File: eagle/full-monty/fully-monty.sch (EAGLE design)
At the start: 20 parts

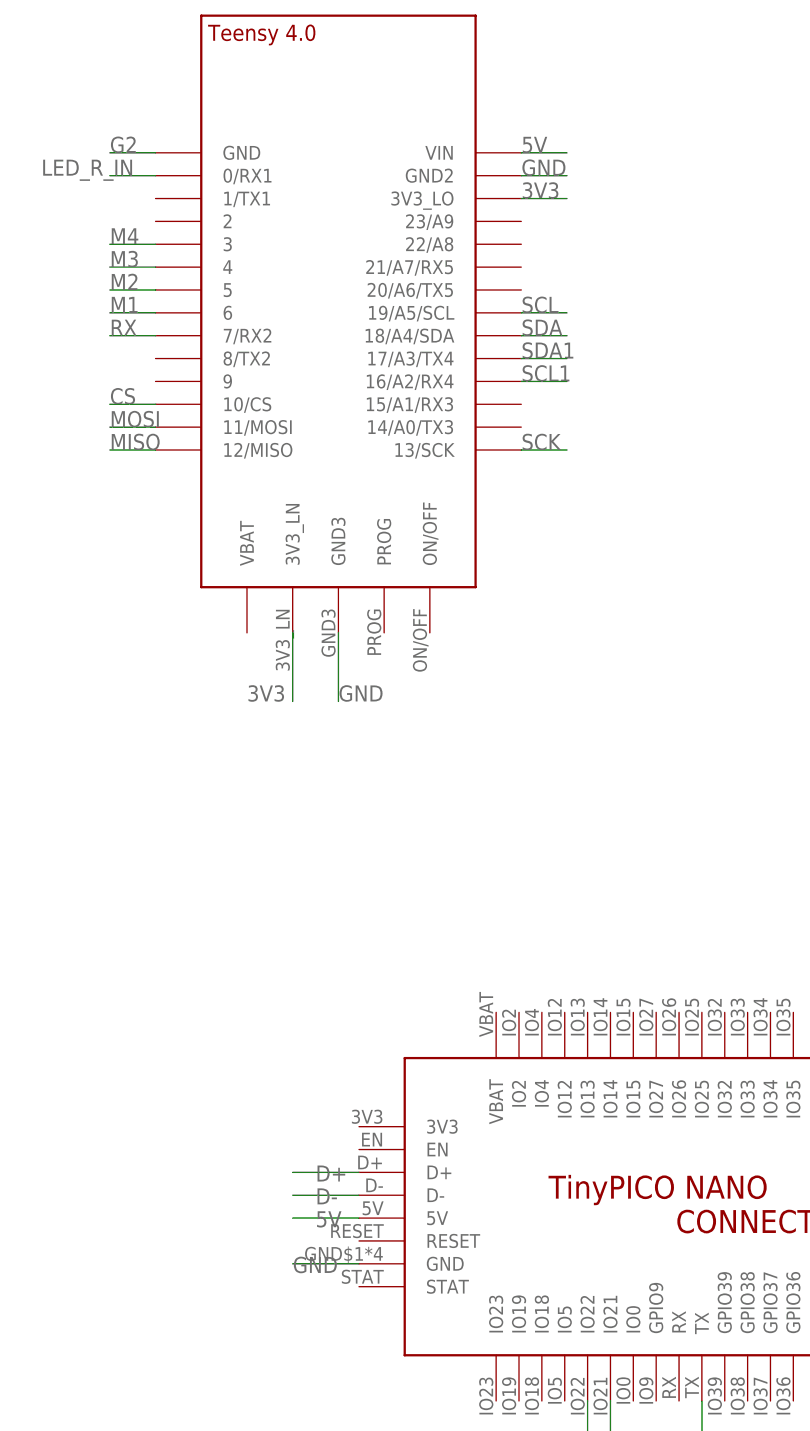
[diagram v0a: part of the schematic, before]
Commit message: modified:   eagle/full-monty/fully-monty.brd
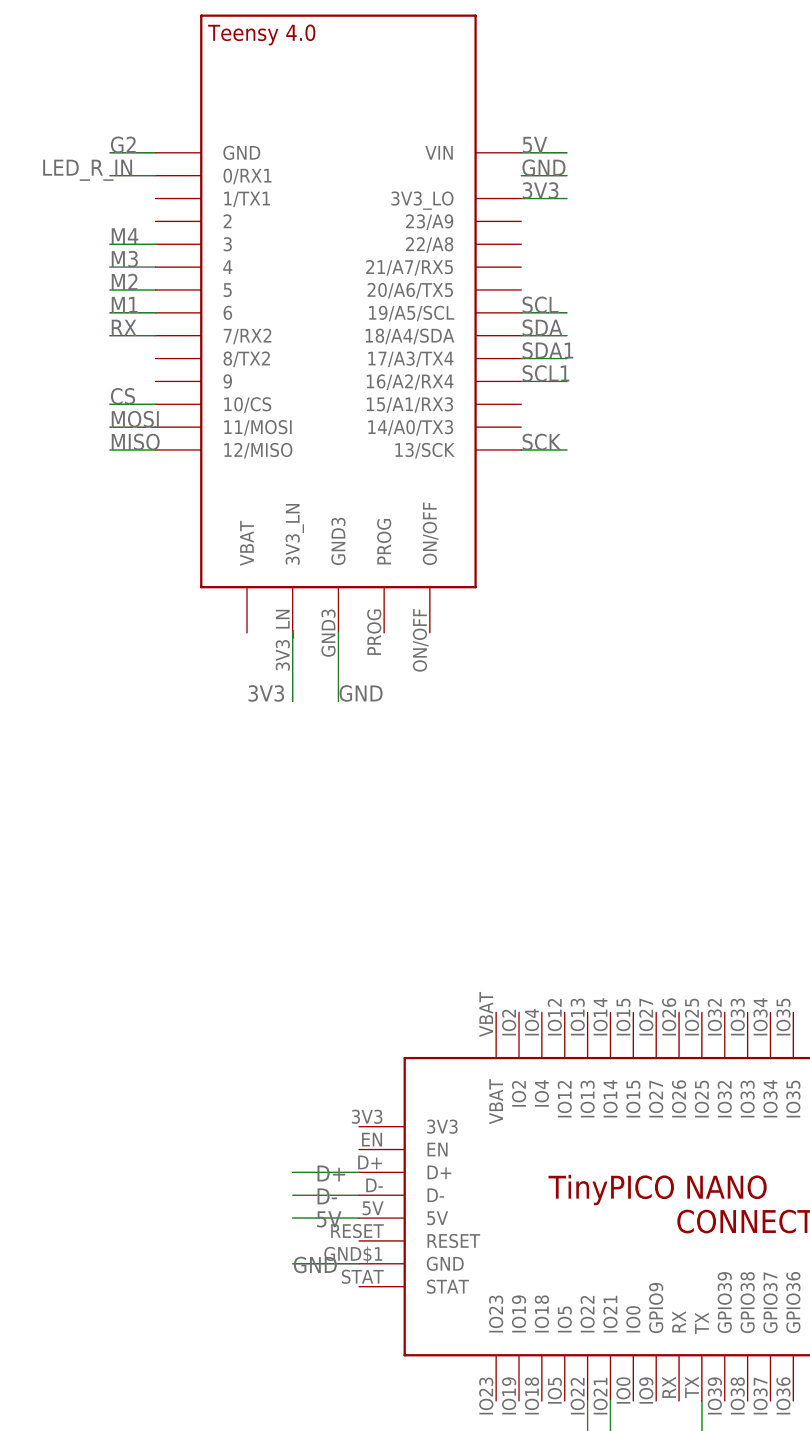
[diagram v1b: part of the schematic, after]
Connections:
- net GND: no longer U$1.GND2
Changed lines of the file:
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@@
 <net name="GND" class="0">
 <segment>
-<pinref part="U$1" gate="G$1" pin="GND2"/>
 <wire x1="93.98" y1="60.96" x2="99.06" y2="60.96" width="0.1524" layer="91"/>
 <label x="93.98" y="60.96" size="1.778" layer="95"/>

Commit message: modified:   fully-monty.brd
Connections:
- net GND: now also U$1.GND2
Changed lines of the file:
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@@
 <net name="GND" class="0">
-<segment>
-<wire x1="93.98" y1="60.96" x2="99.06" y2="60.96" width="0.1524" layer="91"/>
-<label x="93.98" y="60.96" size="1.778" layer="95"/>
-</segment>
 <segment>
 <pinref part="REG" gate="J1" pin="2"/>
@@
 <label x="213.36" y="50.8" size="1.778" layer="95"/>
 </segment>
+<segment>
+<pinref part="U$1" gate="G$1" pin="GND2"/>
+<wire x1="93.98" y1="60.96" x2="99.06" y2="60.96" width="0.1524" layer="91"/>
+<label x="93.98" y="60.96" size="1.778" layer="95"/>
+</segment>
 </net>

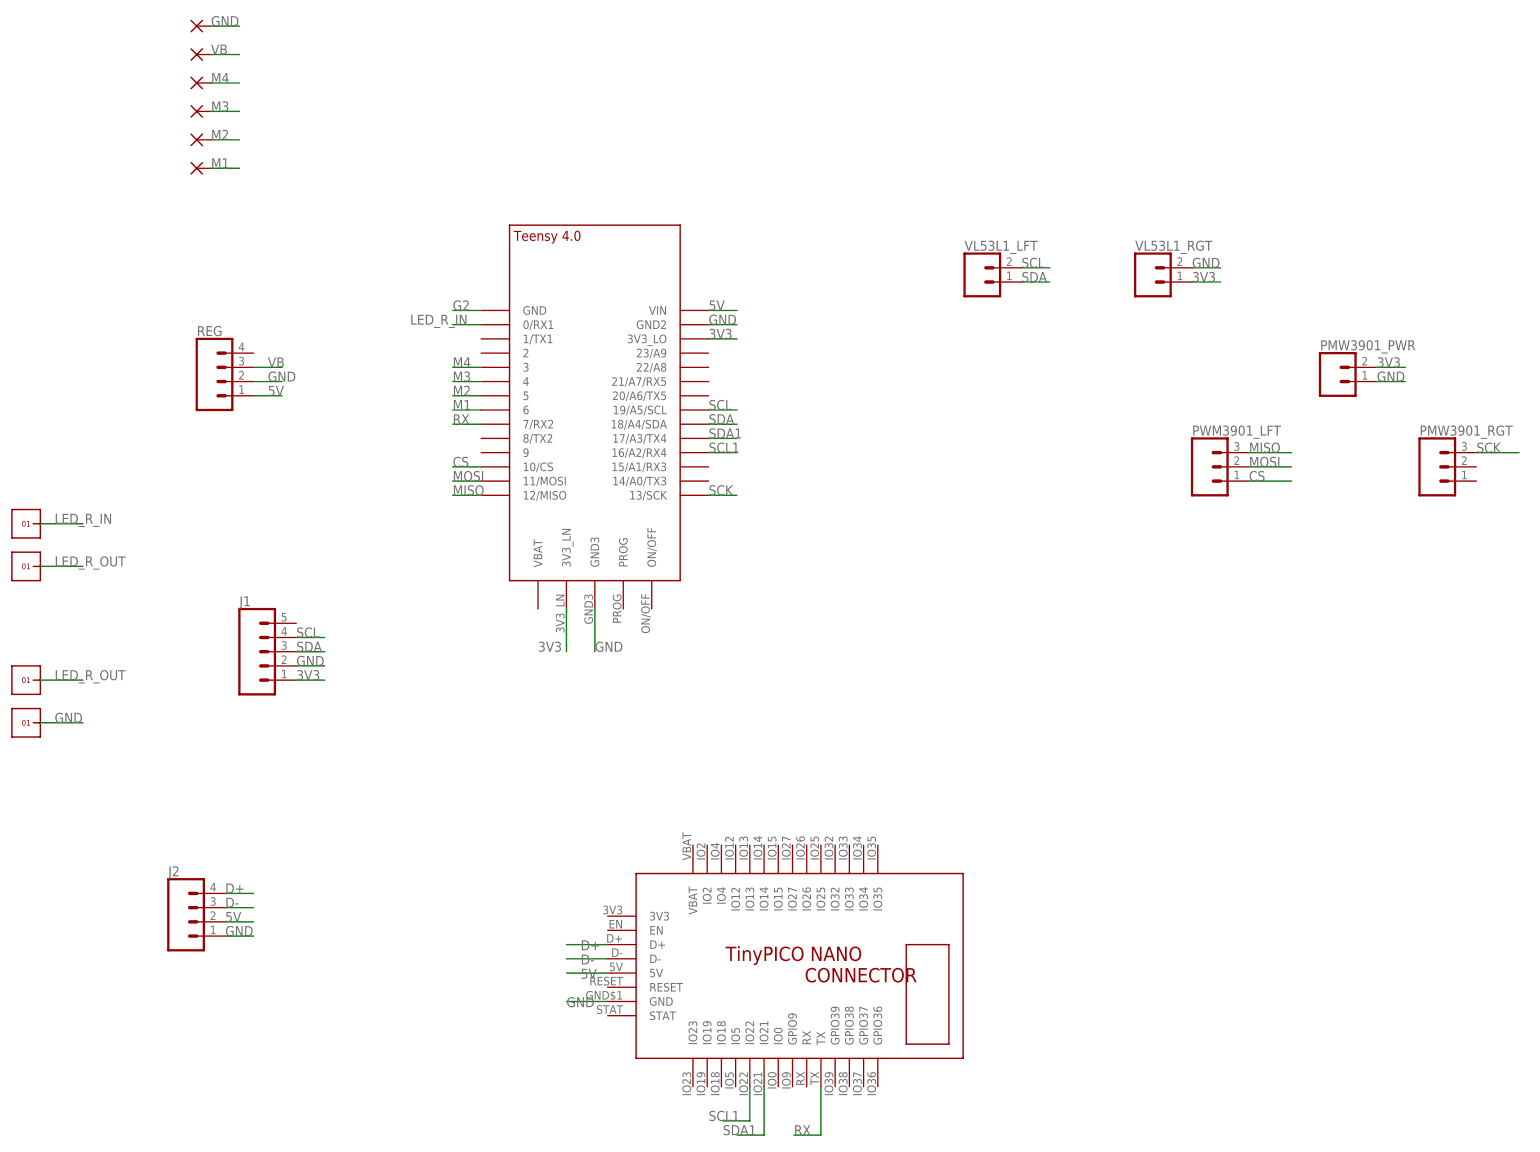
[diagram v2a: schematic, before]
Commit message: modified:   eagle/full-monty/fully-monty.brd
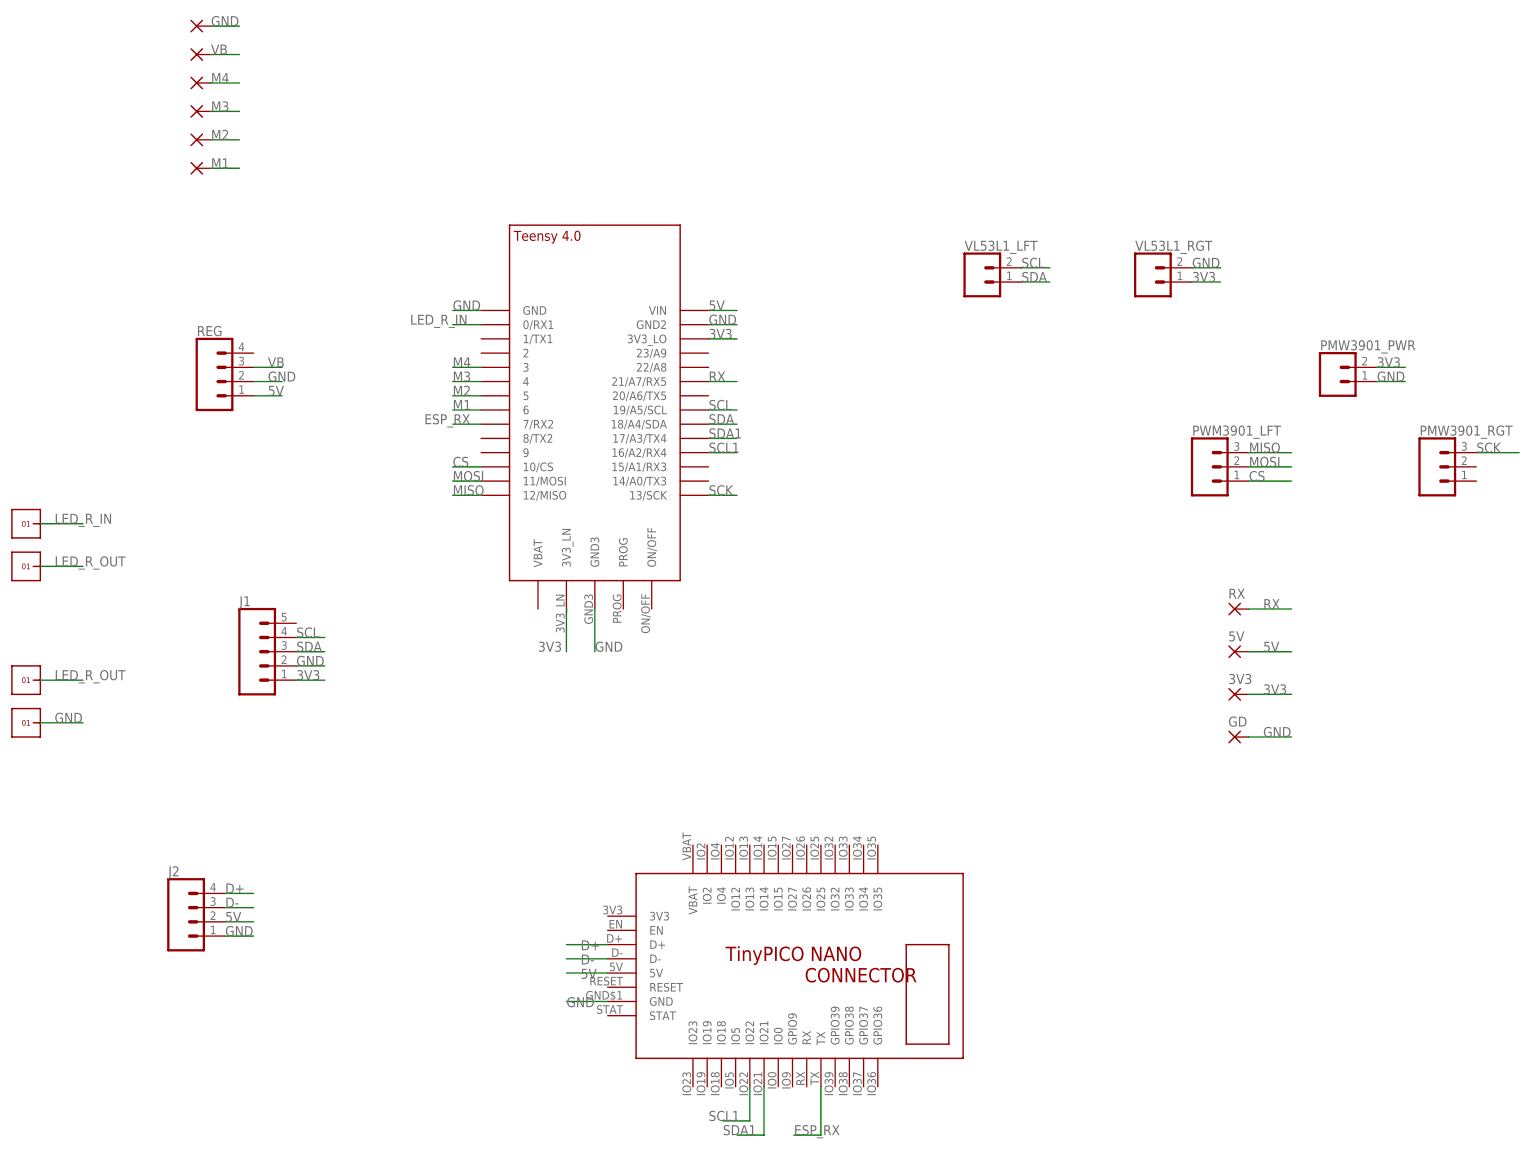
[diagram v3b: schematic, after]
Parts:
- added 3V3, 5V, GD, RX: (no value), wirepad:SMD2
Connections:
- removed net G2: U$1.GND
- new net ESP_RX: U$1.7/RX2, U$2.TX
- net 3V3: now also 3V3.P
- net 5V: now also 5V.P
- net GND: now also GD.P, U$1.GND
- net RX: now also RX.P, U$1.21/A7/RX5; no longer U$1.7/RX2, U$2.TX
